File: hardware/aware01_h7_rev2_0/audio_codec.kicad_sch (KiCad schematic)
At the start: 15 parts, among them IC5 TLV320AIC3204IRHBR

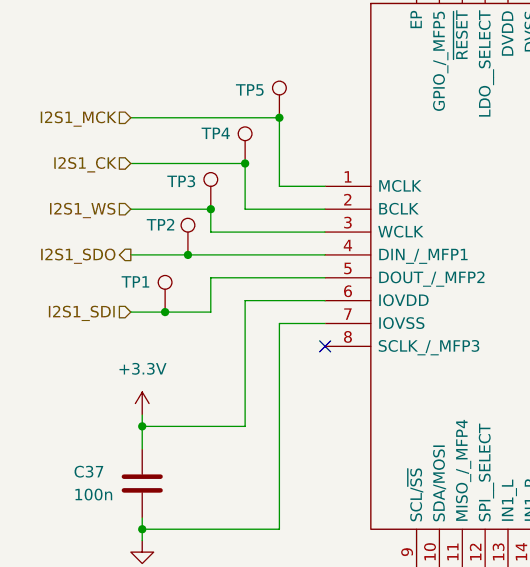
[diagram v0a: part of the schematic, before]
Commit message: hw: add scope screenshots that document buck restart
Which was caused because of short circuit on the MCU pins.
When the LDO received voltage above dropout level, the short draws too
much current and causes the buck to restart.
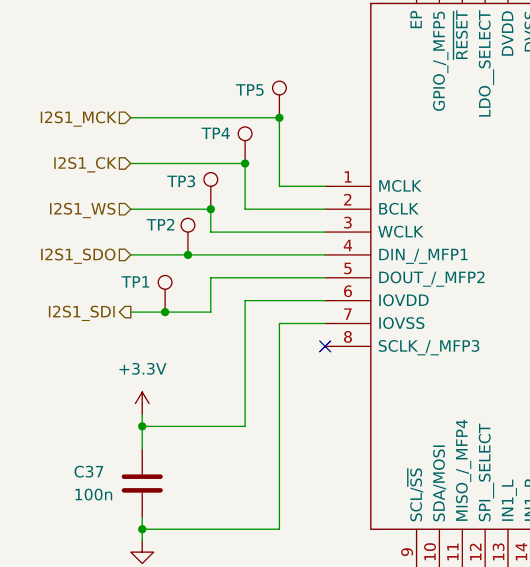
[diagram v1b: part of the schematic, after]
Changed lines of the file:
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@@
 	)
 	(hierarchical_label "I2S1_SDI"
-		(shape input)
+		(shape output)
 		(at 77.47 99.06 180)
 		(effects
@@
 	)
 	(hierarchical_label "I2S1_SDO"
-		(shape output)
+		(shape input)
 		(at 77.47 92.71 180)
 		(effects

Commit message: hw: update schematic
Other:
- company: Ausschussware -> Aware Modular

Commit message: update hardware repo
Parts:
- renumbered TP4 to TP_CK, TP5 to TP_MCK, TP1 to TP_SDI, TP2 to TP_SDO, TP3 to TP_WS
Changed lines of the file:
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@@
 		(in_pos_files yes)
 		(dnp no)
-		(property "Reference" "TP2"
-			(at 79.248 89.408 0)
+		(property "Reference" "TP_SDO"
+			(at 75.438 89.408 0)
 			(show_name no)
 			(do_not_autoplace no)
@@
 			(project "aware01_h7_rev2_0"
 				(path "/efd43d7c-3c18-45dd-8fa5-4bf32165850f/50dd69da-5058-483c-924f-252f04b072bd"
-					(reference "TP2")
+					(reference "TP_SDO")
 					(unit 1)
 				)
@@
 		(in_pos_files yes)
 		(dnp no)
-		(fields_autoplaced yes)
 		(property "Reference" "C39"
-			(at 129.54 124.46 90)
+			(at 129.54 125.222 90)
 			(show_name no)
 			(do_not_autoplace no)
@@
 		)
 		(property "Value" "100n"
-			(at 129.54 127 90)
+			(at 129.54 127.762 90)
 			(show_name no)
 			(do_not_autoplace no)
@@
 		(in_pos_files yes)
 		(dnp no)
-		(property "Reference" "TP4"
-			(at 85.344 79.248 0)
+		(property "Reference" "TP_CK"
+			(at 83.312 79.248 0)
 			(show_name no)
 			(do_not_autoplace no)
@@
 			(project "aware01_h7_rev2_0"
 				(path "/efd43d7c-3c18-45dd-8fa5-4bf32165850f/50dd69da-5058-483c-924f-252f04b072bd"
-					(reference "TP4")
+					(reference "TP_CK")
 					(unit 1)
 				)
@@
 		(in_pos_files yes)
 		(dnp no)
-		(property "Reference" "TP1"
-			(at 76.454 95.758 0)
+		(property "Reference" "TP_SDI"
+			(at 73.66 95.758 0)
 			(show_name no)
 			(do_not_autoplace no)
@@
 			(project "aware01_h7_rev2_0"
 				(path "/efd43d7c-3c18-45dd-8fa5-4bf32165850f/50dd69da-5058-483c-924f-252f04b072bd"
-					(reference "TP1")
+					(reference "TP_SDI")
 					(unit 1)
 				)
@@
 		(in_pos_files yes)
 		(dnp no)
-		(property "Reference" "TP5"
-			(at 89.154 74.422 0)
+		(property "Reference" "TP_MCK"
+			(at 85.598 74.168 0)
 			(show_name no)
 			(do_not_autoplace no)
@@
 			(project "aware01_h7_rev2_0"
 				(path "/efd43d7c-3c18-45dd-8fa5-4bf32165850f/50dd69da-5058-483c-924f-252f04b072bd"
-					(reference "TP5")
+					(reference "TP_MCK")
 					(unit 1)
 				)
@@
 		(in_pos_files yes)
 		(dnp no)
-		(property "Reference" "TP3"
-			(at 81.534 84.582 0)
+		(property "Reference" "TP_WS"
+			(at 79.248 84.328 0)
 			(show_name no)
 			(do_not_autoplace no)
@@
 			(project "aware01_h7_rev2_0"
 				(path "/efd43d7c-3c18-45dd-8fa5-4bf32165850f/50dd69da-5058-483c-924f-252f04b072bd"
-					(reference "TP3")
-					(unit 1)
-				)
+					(reference "TP_WS")
+					(unit 1)
+				)
